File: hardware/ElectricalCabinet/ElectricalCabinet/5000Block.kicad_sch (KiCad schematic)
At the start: 0 parts

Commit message: More updates
Added drawing sheets, wire label scheme, signal list, and traffic light label image to docs folder
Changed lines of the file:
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@@
 	(global_label "5000-1"
 		(shape input)
-		(at 60.96 6.35 180)
+		(at 55.88 6.35 180)
 		(effects
 			(font
@@
 		)
 		(property "Intersheetrefs" "109"
-			(at 50.3549 6.35 0)
+			(at 45.2749 6.35 0)
 			(hide yes)
 			(show_name no)
@@
 		)
 		(property "Ref" "Ref 109"
-			(at 50.8 6.35 0)
+			(at 45.72 6.35 0)
 			(show_name no)
 			(do_not_autoplace no)
@@
 	(global_label "5000-3"
 		(shape input)
-		(at 60.96 13.97 180)
+		(at 55.88 13.97 180)
 		(effects
 			(font
@@
 		)
 		(property "Intersheetrefs" "333"
-			(at 50.3549 13.97 0)
+			(at 45.2749 13.97 0)
 			(hide yes)
 			(show_name no)
@@
 		)
 		(property "Ref" "Ref 333"
-			(at 42.926 13.97 0)
+			(at 37.846 13.97 0)
 			(show_name no)
 			(do_not_autoplace no)
@@
 	(global_label "5000-2"
 		(shape input)
-		(at 60.96 10.16 180)
+		(at 55.88 10.16 180)
 		(effects
 			(font
@@
 		)
 		(property "Intersheetrefs" "212"
-			(at 50.3549 10.16 0)
+			(at 45.2749 10.16 0)
 			(hide yes)
 			(show_name no)
@@
 		)
 		(property "Ref" "Ref 212"
-			(at 42.926 10.16 0)
+			(at 37.846 10.16 0)
 			(show_name no)
 			(do_not_autoplace no)

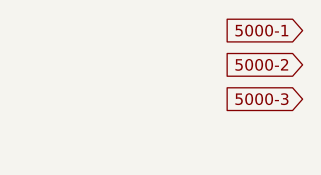
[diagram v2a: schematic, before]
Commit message: Further wiring updates
Populated 6100 Bus
Corrected number of relay boards
Added 110v outputs to relay boards and noted light positon
Uploaded light scheme to documents folder
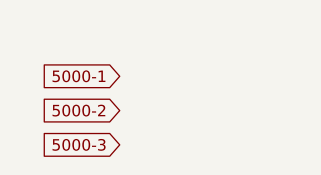
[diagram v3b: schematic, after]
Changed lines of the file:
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@@
 	(generator "eeschema")
 	(generator_version "10.0")
-	(paper "A4")
+	(paper "USLetter")
 	(global_label "5000-1"
 		(shape input)
-		(at 55.88 6.35 180)
+		(at 35.56 11.43 180)
 		(effects
 			(font
@@
 		)
 		(property "Intersheetrefs" "109"
-			(at 45.2749 6.35 0)
+			(at 24.9549 11.43 0)
 			(hide yes)
 			(show_name no)
@@
 		)
 		(property "Ref" "Ref 109"
-			(at 45.72 6.35 0)
+			(at 25.4 11.43 0)
 			(show_name no)
 			(do_not_autoplace no)
@@
 	(global_label "5000-3"
 		(shape input)
-		(at 55.88 13.97 180)
+		(at 35.56 19.05 180)
 		(effects
 			(font
@@
 		)
 		(property "Intersheetrefs" "333"
-			(at 45.2749 13.97 0)
+			(at 24.9549 19.05 0)
 			(hide yes)
 			(show_name no)
@@
 		)
 		(property "Ref" "Ref 333"
-			(at 37.846 13.97 0)
+			(at 17.526 19.05 0)
 			(show_name no)
 			(do_not_autoplace no)
@@
 	(global_label "5000-2"
 		(shape input)
-		(at 55.88 10.16 180)
+		(at 35.56 15.24 180)
 		(effects
 			(font
@@
 		)
 		(property "Intersheetrefs" "212"
-			(at 45.2749 10.16 0)
+			(at 24.9549 15.24 0)
 			(hide yes)
 			(show_name no)
@@
 		)
 		(property "Ref" "Ref 212"
-			(at 37.846 10.16 0)
+			(at 17.526 15.24 0)
 			(show_name no)
 			(do_not_autoplace no)

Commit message: Electrical Cabinet done
Electrical Cabinet done, let me know if there are any changes or mistakes.
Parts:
- added U77, U78, U79, U80, U81, U82, U83: (no value), symbol TrafficLightLibrary:Terminal_Block
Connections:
- net 5000-1: now also U77. (2)
- net 5000-2: now also U78. (2)
- net 5000-3: now also U79. (2)
- new net: U77. (2), U78. (2), U79. (2), U80. (2), U81. (2), U82. (2), U83. (2)
- new net 5000-10: U80. (2)
- new net 5000-11: U79. (2)
- new net 5000-12: U78. (2)
- new net 5000-13: U77. (2)
- new net 5000-4: U80. (2)
- new net 5000-5: U81. (2)
- new net 5000-6: U82. (2)
- new net 5000-7: U83. (2)
- new net 5000-8: U82. (2)
- new net 5000-9: U81. (2)
